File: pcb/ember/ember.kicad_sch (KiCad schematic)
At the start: 34 parts, among them IC5 M24C64-RMN6TP, J1 Conn_01x04_Socket, J2 USB_C_Receptacle_USB2.0, SW1 RESET, SW2 BOOT, U33 AMS1117-3.3, U34 SRV05-4, Y1 16MHz

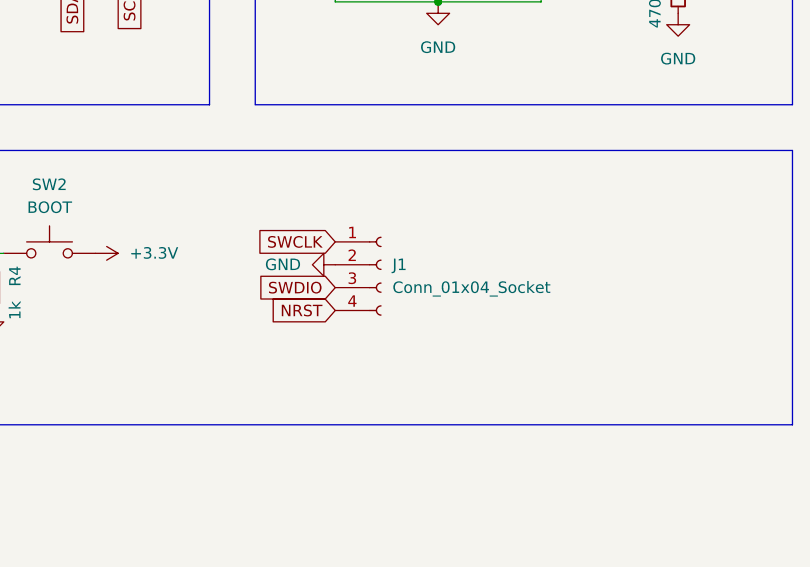
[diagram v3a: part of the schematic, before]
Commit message: :wrench: add VTref Pin
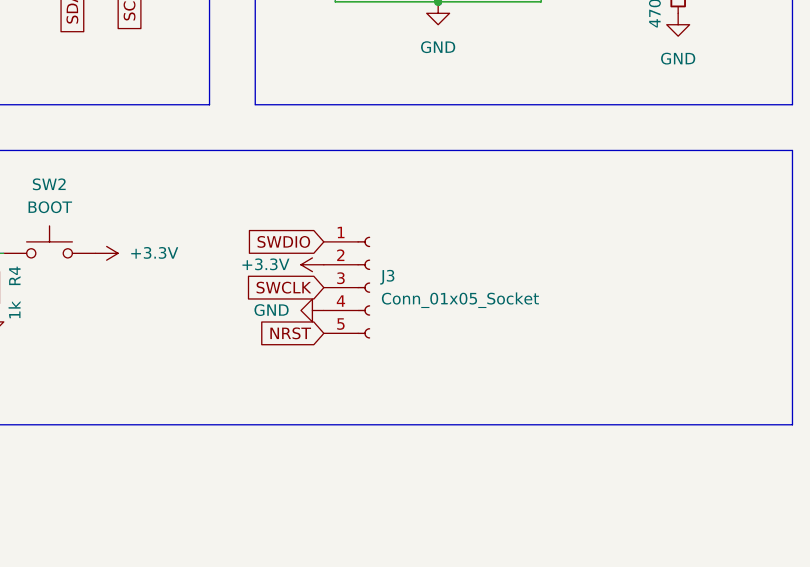
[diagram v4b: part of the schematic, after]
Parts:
- removed J1: Conn_01x04_Socket, Connector_PinSocket_2.54mm:PinSocket_1x04_P2.54mm_Vertical, symbol Connector:Conn_01x04_Socket
- added J3: Conn_01x05_Socket, Connector_PinSocket_2.54mm:PinSocket_1x05_P2.54mm_Vertical, symbol Connector:Conn_01x05_Socket
- J2: LCSC (none) -> C319148
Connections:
- net +3.3V: now also J3.2 (Pin_2)
- net GND: now also J3.4 (Pin_4)
- net NRST: now also J3.5 (Pin_5)
- net SWCLK: now also J3.3 (Pin_3)
- net SWDIO: now also J3.1 (Pin_1)
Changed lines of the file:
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@@
-    )
-  )
-  (global_label "SWCLK" (shape input) (at 228.6 142.24 180) (fields_autoplaced)
-    (effects (font (size 1.27 1.27)) (justify right))
-    (property "Intersheetrefs" "${INTERSHEET_REFS}" (at 219.3858 142.24 0)
-      (effects (font (size 1.27 1.27)) (justify right) hide)
-    )
-  )
-  (global_label "SWDIO" (shape input) (at 228.6 147.32 180) (fields_autoplaced)
-    (effects (font (size 1.27 1.27)) (justify right))
-    (property "Intersheetrefs" "${INTERSHEET_REFS}" (at 219.7486 147.32 0)
-      (effects (font (size 1.27 1.27)) (justify right) hide)
     )
   )
@@
     )
   )
+  (global_label "SWCLK" (shape input) (at 227.33 147.32 180) (fields_autoplaced)
+    (effects (font (size 1.27 1.27)) (justify right))
+    (property "Intersheetrefs" "${INTERSHEET_REFS}" (at 218.1158 147.32 0)
+      (effects (font (size 1.27 1.27)) (justify right) hide)
+    )
+  )
   (global_label "NRST" (shape input) (at 166.37 143.51 180) (fields_autoplaced)
     (effects (font (size 1.27 1.27)) (justify right))
@@
     )
   )
-  (global_label "NRST" (shape input) (at 228.6 149.86 180) (fields_autoplaced)
-    (effects (font (size 1.27 1.27)) (justify right))
-    (property "Intersheetrefs" "${INTERSHEET_REFS}" (at 220.8372 149.86 0)
-      (effects (font (size 1.27 1.27)) (justify right) hide)
-    )
-  )
   (global_label "RCC_OSC_IN" (shape input) (at 101.6 71.12 90) (fields_autoplaced)
     (effects (font (size 1.27 1.27)) (justify left))
@@
     )
   )
+  (global_label "NRST" (shape input) (at 227.33 152.4 180) (fields_autoplaced)
+    (effects (font (size 1.27 1.27)) (justify right))
+    (property "Intersheetrefs" "${INTERSHEET_REFS}" (at 219.5672 152.4 0)
+      (effects (font (size 1.27 1.27)) (justify right) hide)
+    )
+  )
+  (global_label "SWDIO" (shape input) (at 227.33 142.24 180) (fields_autoplaced)
+    (effects (font (size 1.27 1.27)) (justify right))
+    (property "Intersheetrefs" "${INTERSHEET_REFS}" (at 218.4786 142.24 0)
+      (effects (font (size 1.27 1.27)) (justify right) hide)
+    )
+  )
   (global_label "RCC_OSC_OUT" (shape input) (at 116.84 71.12 90) (fields_autoplaced)
     (effects (font (size 1.27 1.27)) (justify left))
@@
         (path "/677b9f05-bf95-4903-b139-ff3eec86ab18"
           (reference "R4") (unit 1)
+        )
+      )
+    )
+  )
+  (symbol (lib_id "Connector:Conn_01x05_Socket") (at 232.41 147.32 0) (unit 1)
+    (in_bom yes) (on_board yes) (dnp no) (fields_autoplaced)
+    (property "Reference" "J3" (at 233.68 146.05 0)
+      (effects (font (size 1.27 1.27)) (justify left))
+    )
+    (property "Value" "Conn_01x05_Socket" (at 233.68 148.59 0)
+      (effects (font (size 1.27 1.27)) (justify left))
+    )
+    (property "Footprint" "Connector_PinSocket_2.54mm:PinSocket_1x05_P2.54mm_Vertical" (at 232.41 147.32 0)
+      (effects (font (size 1.27 1.27)) hide)
+    )
+    (property "Datasheet" "~" (at 232.41 147.32 0)
+      (effects (font (size 1.27 1.27)) hide)
+    )
+    (pin "1")
+    (pin "2")
+    (pin "3")
+    (pin "4")
+    (pin "5")
+    (instances
+      (project "ember"
+        (path "/677b9f05-bf95-4903-b139-ff3eec86ab18"
+          (reference "J3") (unit 1)
         )
       )
@@
       (effects (font (size 1.27 1.27)) hide)
     )
+    (property "LCSC" "C319148" (at 177.8 55.88 0)
+      (effects (font (size 1.27 1.27)) hide)
+    )
     (pin "A1")
     (pin "A12")
@@
     )
   )
-  (symbol (lib_id "power:GND") (at 228.6 144.78 270) (unit 1)
-    (in_bom yes) (on_board yes) (dnp no) (fields_autoplaced)
-    (property "Reference" "#PWR035" (at 222.25 144.78 0)
-      (effects (font (size 1.27 1.27)) hide)
-    )
-    (property "Value" "GND" (at 224.79 144.78 90)
-      (effects (font (size 1.27 1.27)) (justify right))
-    )
-    (property "Footprint" "" (at 228.6 144.78 0)
-      (effects (font (size 1.27 1.27)) hide)
-    )
-    (property "Datasheet" "" (at 228.6 144.78 0)
-      (effects (font (size 1.27 1.27)) hide)
-    )
-    (pin "1")
-    (instances
-      (project "ember"
-        (path "/677b9f05-bf95-4903-b139-ff3eec86ab18"
-          (reference "#PWR035") (unit 1)
-        )
-      )
-    )
-  )
   (symbol (lib_id "Regulator_Linear:AMS1117-3.3") (at 240.03 107.95 0) (unit 1)
     (in_bom yes) (on_board yes) (dnp no) (fields_autoplaced)
@@
     )
   )
+  (symbol (lib_id "power:GND") (at 227.33 149.86 270) (unit 1)
+    (in_bom yes) (on_board yes) (dnp no) (fields_autoplaced)
+    (property "Reference" "#PWR043" (at 220.98 149.86 0)
+      (effects (font (size 1.27 1.27)) hide)
+    )
+    (property "Value" "GND" (at 223.52 149.86 90)
+      (effects (font (size 1.27 1.27)) (justify right))
+    )
+    (property "Footprint" "" (at 227.33 149.86 0)
+      (effects (font (size 1.27 1.27)) hide)
+    )
+    (property "Datasheet" "" (at 227.33 149.86 0)
+      (effects (font (size 1.27 1.27)) hide)
+    )
+    (pin "1")
+    (instances
+      (project "ember"
+        (path "/677b9f05-bf95-4903-b139-ff3eec86ab18"
+          (reference "#PWR043") (unit 1)
+        )
+      )
+    )
+  )
   (symbol (lib_id "Device:R_Small") (at 199.39 110.49 0) (unit 1)
     (in_bom yes) (on_board yes) (dnp no)
@@
     )
   )
+  (symbol (lib_id "power:+3.3V") (at 227.33 144.78 90) (unit 1)
+    (in_bom yes) (on_board yes) (dnp no) (fields_autoplaced)
+    (property "Reference" "#PWR042" (at 231.14 144.78 0)
+      (effects (font (size 1.27 1.27)) hide)
+    )
+    (property "Value" "+3.3V" (at 223.52 144.78 90)
+      (effects (font (size 1.27 1.27)) (justify left))
+    )
+    (property "Footprint" "" (at 227.33 144.78 0)
+      (effects (font (size 1.27 1.27)) hide)
+    )
+    (property "Datasheet" "" (at 227.33 144.78 0)
+      (effects (font (size 1.27 1.27)) hide)
+    )
+    (pin "1")
+    (instances
+      (project "ember"
+        (path "/677b9f05-bf95-4903-b139-ff3eec86ab18"
+          (reference "#PWR042") (unit 1)
+        )
+      )
+    )
+  )
   (symbol (lib_id "Device:C_Small") (at 111.76 44.45 0) (mirror y) (unit 1)
     (in_bom yes) (on_board yes) (dnp no)
@@
         )
       )
-    )
-  )
-  (symbol (lib_id "Connector:Conn_01x04_Socket") (at 233.68 144.78 0) (unit 1)
-    (in_bom yes) (on_board yes) (dnp no) (fields_autoplaced)
-    (property "Reference" "J1" (at 234.95 144.78 0)
-      (effects (font (size 1.27 1.27)) (justify left))
-    )
-    (property "Value" "Conn_01x04_Socket" (at 234.95 147.32 0)
-      (effects (font (size 1.27 1.27)) (justify left))
-    )
-    (property "Footprint" "Connector_PinSocket_2.54mm:PinSocket_1x04_P2.54mm_Vertical" (at 233.68 144.78 0)
-      (effects (font (size 1.27 1.27)) hide)
-    )
-    (property "Datasheet" "~" (at 233.68 144.78 0)
-      (effects (font (size 1.27 1.27)) hide)
-    )
-    (pin "1")
-    (pin "2")
-    (pin "3")
-    (pin "4")
-    (instances
-      (project "ember"
-        (path "/677b9f05-bf95-4903-b139-ff3eec86ab18"
-          (reference "J1") (unit 1)
-        )
-      )

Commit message: change hall size 3.5mm→2.2mm(M2)
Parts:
- H33, H34, H35, H36, H37, H38: footprint MountingHole:MountingHole_3.5mm -> MountingHole:MountingHole_2.2mm_M2
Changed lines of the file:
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@@
       (effects (font (size 1.27 1.27)) (justify left))
     )
-    (property "Footprint" "MountingHole:MountingHole_3.5mm" (at 63.5 171.45 0)
+    (property "Footprint" "MountingHole:MountingHole_2.2mm_M2" (at 63.5 171.45 0)
       (effects (font (size 1.27 1.27)) hide)
     )
@@
       (effects (font (size 1.27 1.27)) (justify left))
     )
-    (property "Footprint" "MountingHole:MountingHole_3.5mm" (at 83.82 171.45 0)
+    (property "Footprint" "MountingHole:MountingHole_2.2mm_M2" (at 83.82 171.45 0)
       (effects (font (size 1.27 1.27)) hide)
     )
@@
       (effects (font (size 1.27 1.27)) (justify left))
     )
-    (property "Footprint" "MountingHole:MountingHole_3.5mm" (at 83.82 176.53 0)
+    (property "Footprint" "MountingHole:MountingHole_2.2mm_M2" (at 83.82 176.53 0)
       (effects (font (size 1.27 1.27)) hide)
     )
@@
       (effects (font (size 1.27 1.27)) (justify left))
     )
-    (property "Footprint" "MountingHole:MountingHole_3.5mm" (at 63.5 181.61 0)
+    (property "Footprint" "MountingHole:MountingHole_2.2mm_M2" (at 63.5 181.61 0)
       (effects (font (size 1.27 1.27)) hide)
     )
@@
       (effects (font (size 1.27 1.27)) (justify left))
     )
-    (property "Footprint" "MountingHole:MountingHole_3.5mm" (at 83.82 181.61 0)
+    (property "Footprint" "MountingHole:MountingHole_2.2mm_M2" (at 83.82 181.61 0)
       (effects (font (size 1.27 1.27)) hide)
     )
@@
       (effects (font (size 1.27 1.27)) (justify left))
     )
-    (property "Footprint" "MountingHole:MountingHole_3.5mm" (at 63.5 176.53 0)
-      (effects (font (size 1.27 1.27)) hide)
-    )
+    (property "Footprint" "MountingHole:MountingHole_2.2mm_M2" (at 63.5 176.53 0)
+      (effects (font (size 1.27 1.27)) hide)
+    )

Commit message: :sparkles: replace cd4052->ad708
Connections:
- no-connect marks 22 -> 26
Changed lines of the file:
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@@
   (no_connect (at 48.26 73.66))
   (no_connect (at 81.28 58.42))
+  (no_connect (at 81.28 66.04))
+  (no_connect (at 228.6 54.61))
   (no_connect (at 48.26 88.9))
   (no_connect (at 48.26 93.98))
+  (no_connect (at 81.28 63.5))
   (no_connect (at 48.26 58.42))
   (no_connect (at 81.28 53.34))
@@
   (no_connect (at 193.04 68.58))
   (no_connect (at 48.26 76.2))
+  (no_connect (at 228.6 59.69))
   (no_connect (at 48.26 96.52))
   (no_connect (at 170.18 78.74))

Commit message: :sparkles: add bypass cap
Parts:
- added C8: 100n, Capacitor_SMD:C_0603_1608Metric, symbol Device:C_Small
- renumbered C3 to C1, C1 to C10, C4 to C2, C5 to C3, C6 to C4, C7 to C5, C9 to C6, C10 to C7, C2 to C9, D2 to D1, H33 to H1, H36 to H2, H34 to H3, H37 to H4, H35 to H5, H38 to H6, IC5 to IC1, J2 to J1, J3 to J2, R8 to R3, R3 to R4, R7 to R5, R5 to R7, R4 to R8, SW2 to SW1, SW1 to SW2, U34 to U1, U33 to U2
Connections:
- net +3.3V: now also C8.1
- net GND: now also C8.2
- net MUX1_B: now also MCU1.12 (PA2); no longer MCU1.11 (PA1)
- net MUX1_C: now also MCU1.11 (PA1); no longer MCU1.12 (PA2)
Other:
- moved on the sheet: R5, R6

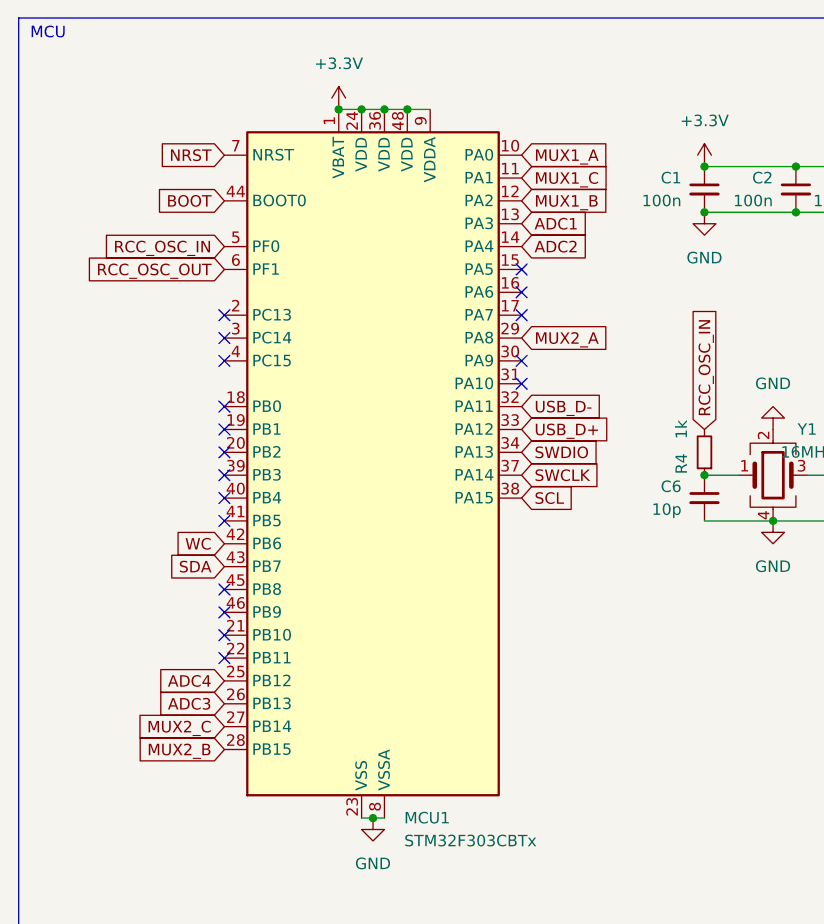
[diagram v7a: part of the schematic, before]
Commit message: :sparkles: opampを使ってのADCに切り替えられるようにピンアサインを変更
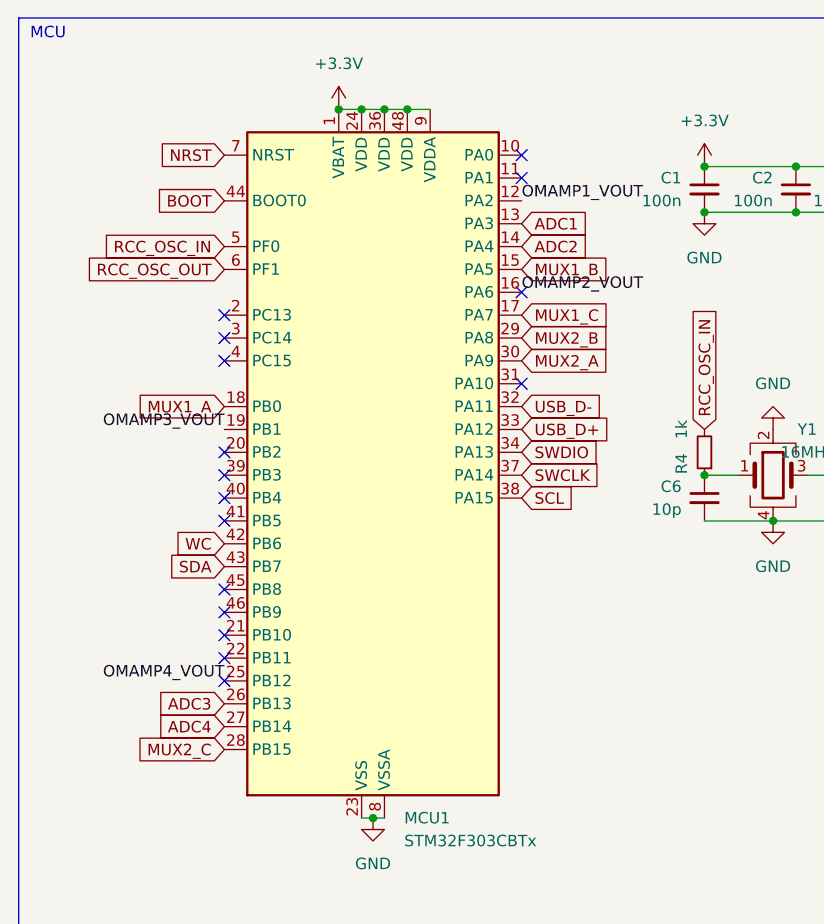
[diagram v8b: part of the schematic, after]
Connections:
- net ADC4: now also MCU1.27 (PB14); no longer MCU1.25 (PB12)
- net MUX1_A: now also MCU1.18 (PB0); no longer MCU1.10 (PA0)
- net MUX1_B: now also MCU1.15 (PA5); no longer MCU1.12 (PA2)
- net MUX1_C: now also MCU1.17 (PA7); no longer MCU1.11 (PA1)
- net MUX2_A: now also MCU1.30 (PA9); no longer MCU1.29 (PA8)
- net MUX2_B: now also MCU1.29 (PA8); no longer MCU1.28 (PB15)
- net MUX2_C: now also MCU1.28 (PB15); no longer MCU1.27 (PB14)
- net OMAMP2_VOUT: now reaches MCU1.16 (PA6)
- net OMAMP3_VOUT: now reaches MCU1.19 (PB1)
- new net OMAMP1_VOUT: MCU1.12 (PA2)
- new net OMAMP4_VOUT: MCU1.25 (PB12)
- no-connect marks 26 -> 24
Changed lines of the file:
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@@
   (no_connect (at 48.26 78.74))
   (no_connect (at 48.26 73.66))
-  (no_connect (at 81.28 58.42))
+  (no_connect (at 81.28 55.88))
   (no_connect (at 81.28 66.04))
   (no_connect (at 228.6 54.61))
   (no_connect (at 48.26 88.9))
   (no_connect (at 48.26 93.98))
-  (no_connect (at 81.28 63.5))
   (no_connect (at 48.26 58.42))
-  (no_connect (at 81.28 53.34))
-  (no_connect (at 48.26 68.58))
   (no_connect (at 193.04 68.58))
   (no_connect (at 48.26 76.2))
   (no_connect (at 228.6 59.69))
   (no_connect (at 48.26 96.52))
+  (no_connect (at 81.28 43.18))
   (no_connect (at 170.18 78.74))
   (no_connect (at 193.04 71.12))
   (no_connect (at 48.26 60.96))
-  (no_connect (at 81.28 55.88))
   (no_connect (at 160.02 113.03))
+  (no_connect (at 48.26 99.06))
   (no_connect (at 48.26 91.44))
   (no_connect (at 48.26 63.5))
   (no_connect (at 160.02 107.95))
+  (no_connect (at 81.28 40.64))
   (no_connect (at 48.26 81.28))
   (no_connect (at 160.02 110.49))
-  (no_connect (at 48.26 71.12))
   (wire (pts (xy 228.6 115.57) (xy 240.03 115.57))
     (stroke (width 0) (type default))
@@
     (effects (font (size 1.27 1.27)) (justify left bottom))
   )
-  (global_label "MUX1_C" (shape input) (at 81.28 43.18 0) (fields_autoplaced)
-    (effects (font (size 1.27 1.27)) (justify left))
-    (property "Intersheetrefs" "${INTERSHEET_REFS}" (at 91.7037 43.18 0)
+  (label "OMAMP3_VOUT" (at 48.26 71.12 180) (fields_autoplaced)
+    (effects (font (size 1.27 1.27)) (justify right bottom))
+  )
+  (label "OMAMP2_VOUT" (at 81.28 55.88 0) (fields_autoplaced)
+    (effects (font (size 1.27 1.27)) (justify left bottom))
+  )
+  (label "OMAMP4_VOUT" (at 48.26 99.06 180) (fields_autoplaced)
+    (effects (font (size 1.27 1.27)) (justify right bottom))
+  )
+  (label "OMAMP1_VOUT" (at 81.28 45.72 0) (fields_autoplaced)
+    (effects (font (size 1.27 1.27)) (justify left bottom))
+  )
+  (global_label "MUX1_C" (shape input) (at 81.28 58.42 0) (fields_autoplaced)
+    (effects (font (size 1.27 1.27)) (justify left))
+    (property "Intersheetrefs" "${INTERSHEET_REFS}" (at 91.7037 58.42 0)
       (effects (font (size 1.27 1.27)) (justify left) hide)
     )
@@
     )
   )
-  (global_label "MUX2_A" (shape input) (at 81.28 60.96 0) (fields_autoplaced)
-    (effects (font (size 1.27 1.27)) (justify left))
-    (property "Intersheetrefs" "${INTERSHEET_REFS}" (at 91.5223 60.96 0)
+  (global_label "MUX2_A" (shape input) (at 81.28 63.5 0) (fields_autoplaced)
+    (effects (font (size 1.27 1.27)) (justify left))
+    (property "Intersheetrefs" "${INTERSHEET_REFS}" (at 91.5223 63.5 0)
       (effects (font (size 1.27 1.27)) (justify left) hide)
     )
@@
     )
   )
-  (global_label "MUX1_B" (shape input) (at 81.28 45.72 0) (fields_autoplaced)
-    (effects (font (size 1.27 1.27)) (justify left))
-    (property "Intersheetrefs" "${INTERSHEET_REFS}" (at 91.7037 45.72 0)
+  (global_label "MUX1_B" (shape input) (at 81.28 53.34 0) (fields_autoplaced)
+    (effects (font (size 1.27 1.27)) (justify left))
+    (property "Intersheetrefs" "${INTERSHEET_REFS}" (at 91.7037 53.34 0)
       (effects (font (size 1.27 1.27)) (justify left) hide)
     )
@@
     )
   )
-  (global_label "MUX2_C" (shape input) (at 48.26 104.14 180) (fields_autoplaced)
-    (effects (font (size 1.27 1.27)) (justify right))
-    (property "Intersheetrefs" "${INTERSHEET_REFS}" (at 37.8363 104.14 0)
+  (global_label "MUX2_C" (shape input) (at 48.26 106.68 180) (fields_autoplaced)
+    (effects (font (size 1.27 1.27)) (justify right))
+    (property "Intersheetrefs" "${INTERSHEET_REFS}" (at 37.8363 106.68 0)
       (effects (font (size 1.27 1.27)) (justify right) hide)
     )
@@
     )
   )
-  (global_label "ADC4" (shape input) (at 48.26 99.06 180) (fields_autoplaced)
-    (effects (font (size 1.27 1.27)) (justify right))
-    (property "Intersheetrefs" "${INTERSHEET_REFS}" (at 40.4367 99.06 0)
+  (global_label "ADC4" (shape input) (at 48.26 104.14 180) (fields_autoplaced)
+    (effects (font (size 1.27 1.27)) (justify right))
+    (property "Intersheetrefs" "${INTERSHEET_REFS}" (at 40.4367 104.14 0)
       (effects (font (size 1.27 1.27)) (justify right) hide)
     )
@@
     )
   )
-  (global_label "MUX1_A" (shape input) (at 81.28 40.64 0) (fields_autoplaced)
-    (effects (font (size 1.27 1.27)) (justify left))
-    (property "Intersheetrefs" "${INTERSHEET_REFS}" (at 91.5223 40.64 0)
-      (effects (font (size 1.27 1.27)) (justify left) hide)
+  (global_label "MUX1_A" (shape input) (at 48.26 68.58 180) (fields_autoplaced)
+    (effects (font (size 1.27 1.27)) (justify right))
+    (property "Intersheetrefs" "${INTERSHEET_REFS}" (at 38.0177 68.58 0)
+      (effects (font (size 1.27 1.27)) (justify right) hide)
     )
   )
@@
     )
   )
-  (global_label "MUX2_B" (shape input) (at 48.26 106.68 180) (fields_autoplaced)
-    (effects (font (size 1.27 1.27)) (justify right))
-    (property "Intersheetrefs" "${INTERSHEET_REFS}" (at 37.8363 106.68 0)
-      (effects (font (size 1.27 1.27)) (justify right) hide)
-    )
-  )
+  (global_label "MUX2_B" (shape input) (at 81.28 60.96 0) (fields_autoplaced)
+    (effects (font (size 1.27 1.27)) (justify left))
+    (property "Intersheetrefs" "${INTERSHEET_REFS}" (at 91.7037 60.96 0)
+      (effects (font (size 1.27 1.27)) (justify left) hide)
+    )
+  )
